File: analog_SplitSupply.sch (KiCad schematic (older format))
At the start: 46 parts, among them J1 Conn_01x04, J2 Conn_01x02, J3 Conn_01x02, J4 Conn_01x02, J5 Conn_01x02, U1 TI_LM2734ZMK_NOPB, U2 AD_LT1054CS8#TRPBF, U3 TI_TLV1117CDCY, U4 AD_LT1175CS8#PBF

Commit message: Updated schematic and prelim layout
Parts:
- removed RV2: BOURNS_3299W-1-204LF, DBLS_Resistor:BOURNS_3299W, symbol DBLS_Resistor:BOURNS_3299W-1-204LF
- added J6: Conn_01x04, Pin_Headers:Pin_Header_Straight_1x04_Pitch2.54mm, symbol Connector_Generic:Conn_01x04
- added JP6, JP7: PAD_JUMPER_2PIN_NC, DBLS_Misc:PAD_JUMPER_2PIN_NC, symbol DBLS_Misc:PAD_JUMPER_2PIN_NC
- added RV2: BOURNS_PV37W204C01B00, Potentiometers:Potentiometer_Trimmer_Bourns_3299Y, symbol DBLS_Resistor:BOURNS_PV37W204C01B00
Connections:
- net GND: now also J6.3 (Pin_3), J6.4 (Pin_4)
- net VIN: now also JP7.1
- net VSW+: now also JP6.1; no longer C7.1, D3.1 (K), U3.3 (VI)
- net at R2.1, U2.1 (FB/SHDN): now also RV2.3
- net VPOS_INV_IN: now reaches C1.1, JP1.2, U2.8 (V+)
- net VPOS_INV_IN: now also J6.1 (Pin_1), J6.2 (Pin_2), JP7.2
- net VNEG_LDO_IN: now reaches C10.1, JP2.2, JP3.1, JP4.1, JP5.1, U4.1 (Vin), U4.8 (Vin)
- net at R1.2: now also RV2.2
- new net VPOS_LDO_IN: C7.1, D3.1 (K), JP6.2, U3.3 (VI)
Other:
- moved on the sheet: JP1
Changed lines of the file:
@@
 	7000 2650 6950 2650
-Wire Wire Line
-	6700 2650 6700 2600
 Wire Wire Line
 	6850 2700 6850 2650
 Connection ~ 6850 2650
 Wire Wire Line
-	6850 2650 6700 2650
+	6850 2650 6100 2650
 $Comp
 L DBLS_Diode:VISHAY_SSA33L-E3_61T D3
@@
 Connection ~ 2150 4200
 Wire Wire Line
-	2150 4200 2000 4200
-Wire Wire Line
-	1750 4100 1750 4200
+	2150 4200 1550 4200
+Wire Wire Line
+	1200 4100 1200 4200
 Wire Wire Line
 	3400 4400 3500 4400
@@
 L DBLS_Misc:PAD_JUMPER_2PIN_NC JP1
 U 1 1 624503ED
-P 1900 4200
-F 0 "JP1" H 1800 4100 50  0000 L BNN
-F 1 "PAD_JUMPER_2PIN_NC" H 1950 3900 50  0001 C CNN
-F 2 "DBLS_Misc:PAD_JUMPER_2PIN_NC" H 1900 4400 50  0001 C CNN
-F 3 "" H 1900 4400 50  0001 C CNN
-F 4 "DNI" H 2100 3950 25  0001 C CNN "place"
-	1    1900 4200
-	1    0    0    -1
-$EndComp
-Wire Wire Line
-	1800 4200 1750 4200
+P 1400 4200
+F 0 "JP1" H 1300 4100 50  0000 L BNN
+F 1 "PAD_JUMPER_2PIN_NC" H 1450 3900 50  0001 C CNN
+F 2 "DBLS_Misc:PAD_JUMPER_2PIN_NC" H 1400 4400 50  0001 C CNN
+F 3 "" H 1400 4400 50  0001 C CNN
+F 4 "DNI" H 1600 3950 25  0001 C CNN "place"
+	1    1400 4200
+	1    0    0    -1
+$EndComp
+Wire Wire Line
+	1300 4200 1200 4200
 $Comp
 L DBLS_Misc:PAD_JUMPER_2PIN_NC JP2
@@
 $EndComp
 $Comp
-L DBLS_power:VSW+ #PWR0102
-U 1 1 623FDF2B
-P 6700 2600
-F 0 "#PWR0102" H 6700 2600 50  0001 C CNN
-F 1 "VSW+" H 6700 2750 50  0000 C CNN
-F 2 "" H 6700 2600 50  0001 C CNN
-F 3 "" H 6700 2600 50  0001 C CNN
-	1    6700 2600
-	1    0    0    -1
-$EndComp
-$Comp
 L DBLS_power:VSW+ #PWR0103
 U 1 1 623FE2C8
-P 1750 4100
-F 0 "#PWR0103" H 1750 4100 50  0001 C CNN
-F 1 "VSW+" H 1750 4250 50  0000 C CNN
-F 2 "" H 1750 4100 50  0001 C CNN
-F 3 "" H 1750 4100 50  0001 C CNN
-	1    1750 4100
+P 1200 4100
+F 0 "#PWR0103" H 1200 4100 50  0001 C CNN
+F 1 "VSW+" H 1200 4250 50  0000 C CNN
+F 2 "" H 1200 4100 50  0001 C CNN
+F 3 "" H 1200 4100 50  0001 C CNN
+	1    1200 4100
 	1    0    0    -1
 $EndComp
@@
 	2050 5300 2050 5250
 $Comp
-L DBLS_Resistor:BOURNS_3299W-1-204LF RV2
-U 1 1 62479D4A
-P 2050 5050
-F 0 "RV2" H 1950 5050 50  0000 C CNN
-F 1 "BOURNS_3299W-1-204LF" V 1950 5050 50  0001 C CNN
-F 2 "DBLS_Resistor:BOURNS_3299W" H 2050 5050 50  0001 C CNN
-F 3 "https://www.bourns.com/docs/Product-Datasheets/3299.pdf" H 2050 5050 50  0001 C CNN
-F 4 "Bourns Inc" H 2050 5050 50  0001 C CNN "mfg"
-F 5 "3299W-1-204LF" H 2050 5050 50  0001 C CNN "mfg_pn"
-F 6 "digikey" H 2050 5050 50  0001 C CNN "vendor"
-F 7 "3299W-204LF-ND" H 2050 5050 50  0001 C CNN "vendor_pn"
-F 8 "" H 2050 5050 50  0001 C CNN "place"
-F 9 "200k" H 1850 4950 40  0000 L CNN "resistance"
-F 10 "TRIMMER POT 200K OHM 0.5W PC PIN TOP" H 2050 5050 50  0001 C CNN "description"
-	1    2050 5050
-	-1   0    0    -1
-$EndComp
-$Comp
 L DBLS_Resistor:VISHAYDALE_RCA0603100KFKEAHP R1
 U 1 1 62485F04
@@
 Wire Wire Line
 	4050 4200 4200 4200
+$Comp
+L DBLS_Resistor:BOURNS_PV37W204C01B00 RV2
+U 1 1 6241D697
+P 2050 5050
+F 0 "RV2" H 1950 4950 50  0000 C CNN
+F 1 "BOURNS_PV37W204C01B00" V 1950 5050 50  0001 C CNN
+F 2 "Potentiometers:Potentiometer_Trimmer_Bourns_3299Y" H 2050 5050 50  0001 C CNN
+F 3 "https://www.bourns.com/docs/Product-Datasheets/pv37.pdf" H 2050 5050 50  0001 C CNN
+F 4 "Bourns Inc" H 2050 5050 50  0001 C CNN "mfg"
+F 5 "PV37W204C01B00" H 2050 5050 50  0001 C CNN "mfg_pn"
+F 6 "digikey" H 2050 5050 50  0001 C CNN "vendor"
+F 7 "490-2977-ND" H 2050 5050 50  0001 C CNN "vendor_pn"
+F 8 "" H 2050 5050 50  0001 C CNN "place"
+F 9 "200k" H 1850 4900 40  0000 L CNN "resistance"
+F 10 "TRIMMER 200K OHM 0.25W PC PIN TOP" H 2050 5050 50  0001 C CNN "description"
+	1    2050 5050
+	-1   0    0    -1
+$EndComp
+Text Label 5500 4950 0    50   ~ 0
+VNEG_LDO_IN
+$Comp
+L DBLS_Misc:PAD_JUMPER_2PIN_NC JP6
+U 1 1 6247E110
+P 6000 2650
+F 0 "JP6" H 5900 2550 50  0000 L BNN
+F 1 "PAD_JUMPER_2PIN_NC" H 6050 2350 50  0001 C CNN
+F 2 "DBLS_Misc:PAD_JUMPER_2PIN_NC" H 6000 2850 50  0001 C CNN
+F 3 "" H 6000 2850 50  0001 C CNN
+F 4 "DNI" H 6200 2400 25  0001 C CNN "place"
+	1    6000 2650
+	1    0    0    -1
+$EndComp
+$Comp
+L DBLS_power:VSW+ #PWR031
+U 1 1 6247F135
+P 5750 2550
+F 0 "#PWR031" H 5750 2550 50  0001 C CNN
+F 1 "VSW+" H 5750 2700 50  0000 C CNN
+F 2 "" H 5750 2550 50  0001 C CNN
+F 3 "" H 5750 2550 50  0001 C CNN
+	1    5750 2550
+	1    0    0    -1
+$EndComp
+Wire Wire Line
+	5900 2650 5750 2650
+Wire Wire Line
+	5750 2650 5750 2550
+Text Label 6250 2650 0    50   ~ 0
+VPOS_LDO_IN
+$Comp
+L Connector_Generic:Conn_01x04 J6
+U 1 1 6248EE15
+P 3650 7100
+F 0 "J6" H 3650 7300 50  0000 C CNN
+F 1 "Conn_01x04" H 3650 6800 50  0000 C CNN
+F 2 "Pin_Headers:Pin_Header_Straight_1x04_Pitch2.54mm" H 3650 7100 50  0001 C CNN
+F 3 "~" H 3650 7100 50  0001 C CNN
+	1    3650 7100
+	-1   0    0    -1
+$EndComp
+Text Label 1650 4200 0    50   ~ 0
+VPOS_INV_IN
+Text Label 3950 6850 0    50   ~ 0
+VPOS_INV_IN
+Wire Wire Line
+	3850 7000 3950 7000
+Wire Wire Line
+	3850 7100 3950 7100
+Wire Wire Line
+	3950 7100 3950 7000
+Connection ~ 3950 7000
+Wire Wire Line
+	3950 7000 3950 6850
+Wire Wire Line
+	3850 7200 3950 7200
+Wire Wire Line
+	3950 7200 3950 7300
+Wire Wire Line
+	3850 7300 3950 7300
+Connection ~ 3950 7300
+Wire Wire Line
+	3950 7300 3950 7400
+$Comp
+L power:GND #PWR030
+U 1 1 624B4EC4
+P 3950 7400
+F 0 "#PWR030" H 3950 7150 50  0001 C CNN
+F 1 "GND" H 3950 7250 50  0000 C CNN
+F 2 "" H 3950 7400 50  0001 C CNN
+F 3 "" H 3950 7400 50  0001 C CNN
+	1    3950 7400
+	1    0    0    -1
+$EndComp
+Wire Wire Line
+	1200 3650 1200 3750
+$Comp
+L DBLS_Misc:PAD_JUMPER_2PIN_NC JP7
+U 1 1 62518D21
+P 1400 3750
+F 0 "JP7" H 1300 3650 50  0000 L BNN
+F 1 "PAD_JUMPER_2PIN_NC" H 1450 3450 50  0001 C CNN
+F 2 "DBLS_Misc:PAD_JUMPER_2PIN_NC" H 1400 3950 50  0001 C CNN
+F 3 "" H 1400 3950 50  0001 C CNN
+F 4 "DNI" H 1600 3500 25  0001 C CNN "place"
+	1    1400 3750
+	1    0    0    -1
+$EndComp
+Wire Wire Line
+	1300 3750 1200 3750
+$Comp
+L DBLS_power:VIN #PWR032
+U 1 1 6251E4A8
+P 1200 3650
+F 0 "#PWR032" H 1200 3650 50  0001 C CNN
+F 1 "VIN" H 1200 3800 50  0000 C CNN
+F 2 "" H 1200 3650 50  0001 C CNN
+F 3 "" H 1200 3650 50  0001 C CNN
+	1    1200 3650
+	1    0    0    -1
+$EndComp
+Wire Wire Line
+	1500 3750 1550 3750
+Wire Wire Line
+	1550 3750 1550 4200
+Connection ~ 1550 4200
+Wire Wire Line
+	1550 4200 1500 4200
 $EndSCHEMATC

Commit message: cleaned up silkscreen
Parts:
- added LOGO1: DBLS_van_logo_small_v1, DBLS_LOGO:van_logo_small, symbol DBLS_Logo:DBLS_van_logo_small_v1
- added LOGO2: DBLS_Chicken_Small, DBLS_LOGO:Rooster_4mmx4mm, symbol DBLS_Logo:DBLS_Chicken_Small
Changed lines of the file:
@@
 Wire Wire Line
 	1550 4200 1500 4200
+$Comp
+L DBLS_Logo:DBLS_Chicken_Small LOGO2
+U 1 1 6246F17A
+P 10500 5800
+F 0 "LOGO2" H 10500 5800 50  0001 C CNN
+F 1 "DBLS_Chicken_Small" H 10500 5800 50  0001 C CNN
+F 2 "DBLS_LOGO:Rooster_4mmx4mm" H 10530 5950 20  0001 C CNN
+F 3 "" H 10500 5800 50  0001 C CNN
+F 4 "DNI" H 10500 5800 50  0001 C CNN "place"
+	1    10500 5800
+	1    0    0    -1
+$EndComp
+$Comp
+L DBLS_Logo:DBLS_van_logo_small_v1 LOGO1
+U 1 1 6246F6AD
+P 9950 5800
+F 0 "LOGO1" H 9950 5800 50  0001 C CNN
+F 1 "DBLS_van_logo_small_v1" H 9950 5800 50  0001 C CNN
+F 2 "DBLS_LOGO:van_logo_small" H 9980 5950 20  0001 C CNN
+F 3 "" H 9950 5800 50  0001 C CNN
+F 4 "DNI" H 9950 5800 50  0001 C CNN "place"
+	1    9950 5800
+	1    0    0    -1
+$EndComp
 $EndSCHEMATC

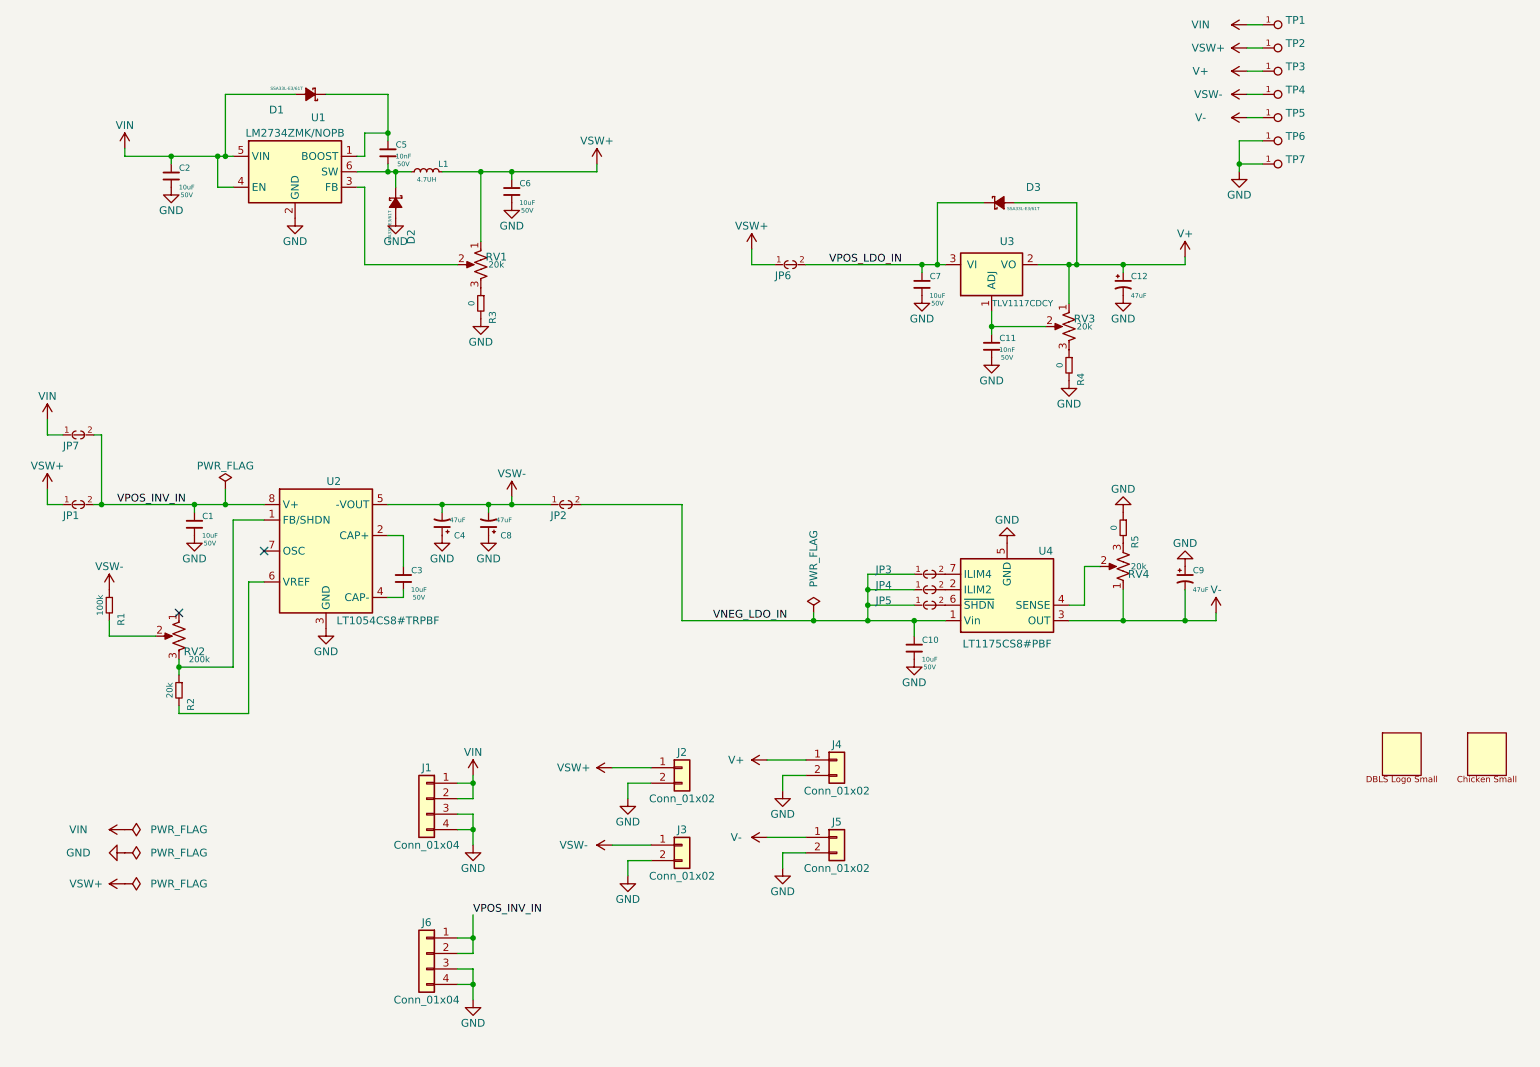
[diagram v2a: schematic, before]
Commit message: Added logos, updated jumpers, and added second set of output headers.
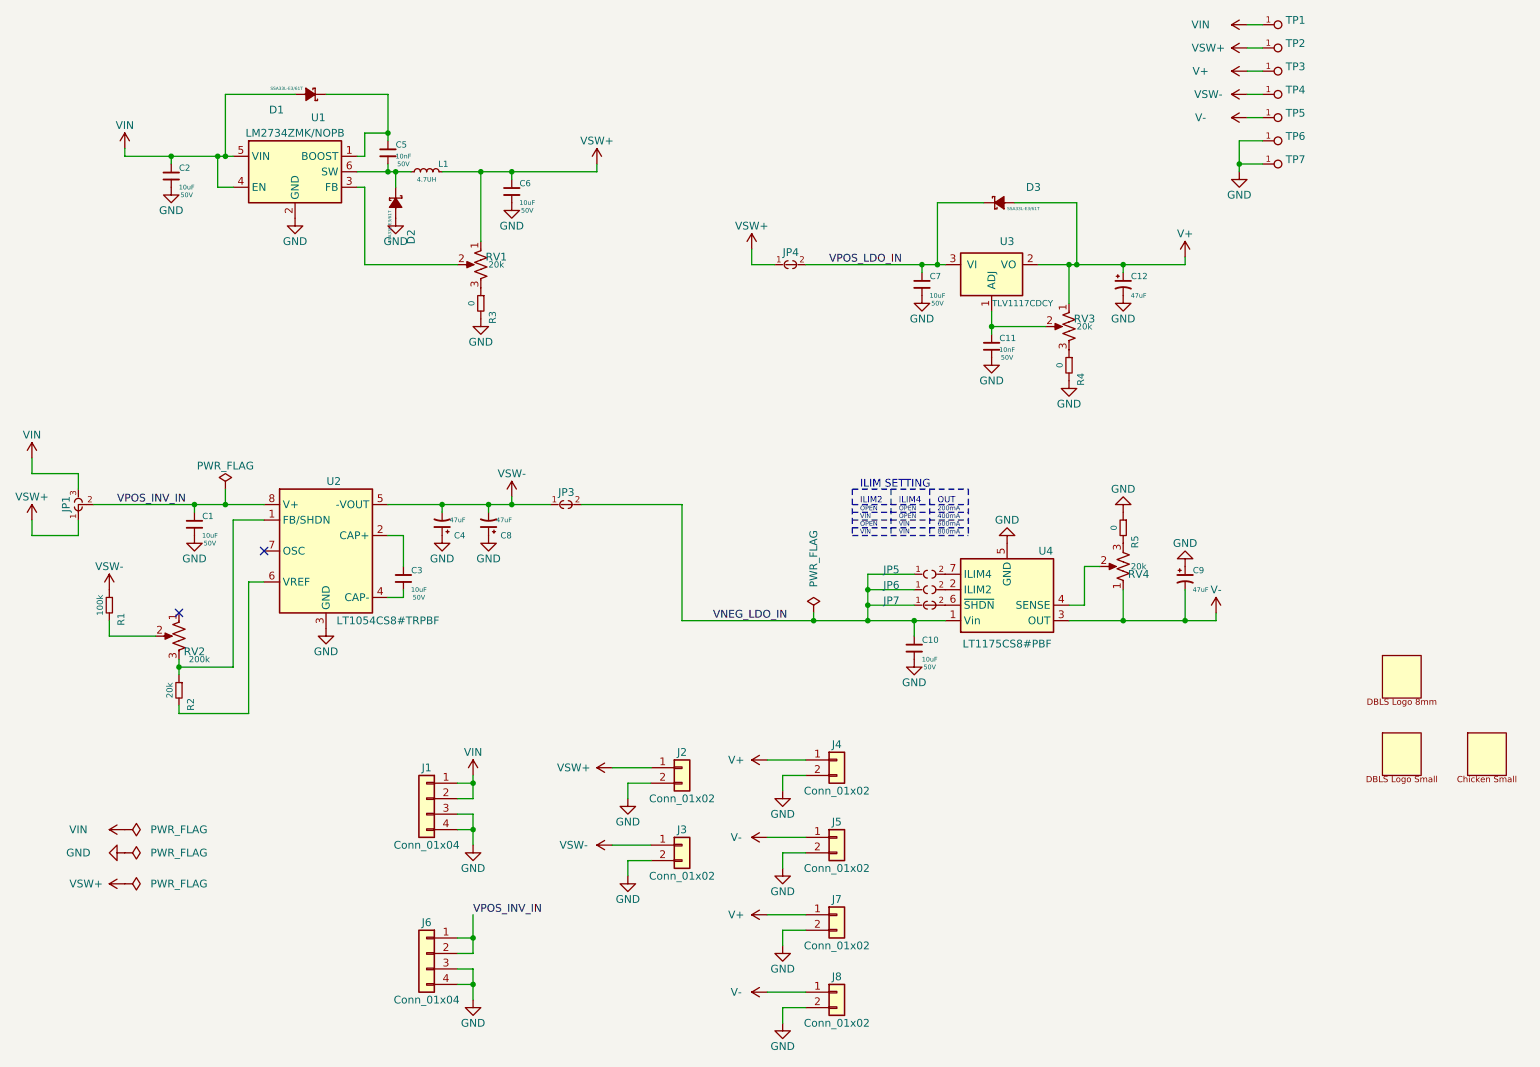
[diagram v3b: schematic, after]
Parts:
- removed JP1, JP2, JP3, JP4, JP5, JP6, JP7: PAD_JUMPER_2PIN_NC, DBLS_Misc:PAD_JUMPER_2PIN_NC, symbol DBLS_Misc:PAD_JUMPER_2PIN_NC
- added J7, J8: Conn_01x02, Pin_Headers:Pin_Header_Straight_1x02_Pitch2.54mm, symbol Connector_Generic:Conn_01x02
- added JP1: PAD_JUMPER_3PIN_12_NC_BY_TRACE, DBLS_Jumpers:PAD_JUMPER_3PIN_12_NC_BY_TRACE, symbol DBLS_Misc:PAD_JUMPER_3PIN_12_NC_BY_TRACE
- added JP3, JP4, JP7: PAD_JUMPER_2PIN_NC_BY_TRACE, DBLS_Jumpers:PAD_JUMPER_2PIN_NC_BY_TRACE, symbol DBLS_Misc:PAD_JUMPER_2PIN_NC_BY_TRACE
- added JP5, JP6: PAD_JUMPER_2PIN_NO, DBLS_Jumpers:PAD_JUMPER_2PIN_NO_0603, symbol DBLS_Misc:PAD_JUMPER_2PIN_NO
- added LOGO3: DBLS_van_logo_8mmX6mm, DBLS_LOGO:van_logo_8mmX6mm, symbol DBLS_Logo:DBLS_van_logo_8mmX6mm
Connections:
- net GND: now also J7.2 (Pin_2), J8.2 (Pin_2)
- net V+: now also J7.1 (Pin_1)
- net V-: now also J8.1 (Pin_1)
- net VIN: now also JP1.3
- net VNEG_LDO_IN: now also JP3.2, JP5.1, JP6.1, JP7.1
- net VPOS_INV_IN: now also JP1.2
- net VPOS_LDO_IN: now also JP4.2
- net VSW+: now also JP1.1, JP4.1
- net VSW-: now also JP3.1
- net at U4.2 (ILIM2): now also JP6.2
- net at U4.6 (~SHDN): now also JP7.2
- net at U4.7 (ILIM4): now also JP5.2
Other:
- note added: "200mA"
- note added: "400mA"
- note added: "600mA"
- note added: "800mA"
- note added: "ILIM SETTING"
- note added: "ILIM2"
- note added: "ILIM4"
- note added: "OPEN"
- note added: "OUT"
- note added: "VIN"
